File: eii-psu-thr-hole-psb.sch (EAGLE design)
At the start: 30 parts, among them IC2 7812TV

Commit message: Switched to through-hole resistors too
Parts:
- +15V, +5V, -15V, G, GND, L, N: value (none) -> PIN2F061.100; device SparkFun-Connectors:CONN_01PTH_2MM -> con-faston:PIN2F061.100
- R1, R2, R3, R4: device rcl:R-EU_R1206 -> rcl:R-EU_0207/7
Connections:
- new net G: G.1, X2-7.S
- net GND: no longer G.1, X2-7.S
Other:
- note added: "C86469"

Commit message: New heat sinks, better silk screen
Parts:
- KK1, KK2, KK3: value SK95V -> HEATSINKXSD; device joakim:SK95V -> joakim:HEATSINKXSD
- renumbered U$1 to IC1, U$2 to IC3
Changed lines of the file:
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@@
 <parts>
 <part name="IC2" library="linear" library_urn="urn:adsk.eagle:library:262" deviceset="78*" device="TV" package3d_urn="urn:adsk.eagle:package:16417/2" technology="12" value="7812TV"/>
-<part name="U$1" library="joakim" deviceset="LD1085V" device="3" value="LD1085V3"/>
-<part name="U$2" library="joakim" deviceset="LM2991" device="V" value="LM2991V"/>
+<part name="IC1" library="joakim" deviceset="LD1085V" device="3" value="LD1085V3"/>
+<part name="IC3" library="joakim" deviceset="LM2991" device="V" value="LM2991V"/>
 <part name="C1" library="rcl" library_urn="urn:adsk.eagle:library:334" deviceset="CPOL-US" device="E5-10.5" package3d_urn="urn:adsk.eagle:package:23372/2" value="470uF"/>
 <part name="C2" library="rcl" library_urn="urn:adsk.eagle:library:334" deviceset="CPOL-US" device="E5-10.5" package3d_urn="urn:adsk.eagle:package:23372/2" value="470uF"/>
@@
 <part name="GND" library="con-faston" library_urn="urn:adsk.eagle:library:144" deviceset="PIN2" device="F061.100" package3d_urn="urn:adsk.eagle:package:6758/1"/>
 <part name="GND15" library="supply1" library_urn="urn:adsk.eagle:library:371" deviceset="GND" device=""/>
-<part name="KK1" library="joakim" deviceset="SK95" device="V"/>
-<part name="KK2" library="joakim" deviceset="SK95" device="V"/>
-<part name="KK3" library="joakim" deviceset="SK95" device="V"/>
+<part name="KK1" library="joakim" deviceset="HEATSINK" device="XSD"/>
+<part name="KK2" library="joakim" deviceset="HEATSINK" device="XSD"/>
+<part name="KK3" library="joakim" deviceset="HEATSINK" device="XSD"/>
 </parts>
 <sheets>
@@
 <attribute name="VALUE" x="55.88" y="61.595" size="1.778" layer="96"/>
 </instance>
-<instance part="U$1" gate="G$1" x="63.5" y="101.6" smashed="yes">
+<instance part="IC1" gate="G$1" x="63.5" y="101.6" smashed="yes">
 <attribute name="NAME" x="55.88" y="107.315" size="1.778" layer="95"/>
 <attribute name="VALUE" x="55.88" y="104.775" size="1.778" layer="96"/>
 </instance>
-<instance part="U$2" gate="G$1" x="63.5" y="27.94" smashed="yes">
+<instance part="IC3" gate="G$1" x="63.5" y="27.94" smashed="yes">
 <attribute name="NAME" x="55.88" y="33.655" size="1.778" layer="95"/>
 <attribute name="VALUE" x="55.88" y="31.115" size="1.778" layer="96"/>
@@
 <net name="N$6" class="0">
 <segment>
-<pinref part="U$2" gate="G$1" pin="ADJ"/>
+<pinref part="IC3" gate="G$1" pin="ADJ"/>
 <wire x1="68.58" y1="20.32" x2="68.58" y2="7.62" width="0.1524" layer="91"/>
 <pinref part="R6" gate="G$1" pin="1"/>
@@
 </segment>
 <segment>
-<pinref part="U$2" gate="G$1" pin="GND"/>
+<pinref part="IC3" gate="G$1" pin="GND"/>
 <pinref part="GND3" gate="1" pin="GND"/>
 </segment>
 <segment>
-<pinref part="U$2" gate="G$1" pin="ON"/>
+<pinref part="IC3" gate="G$1" pin="ON"/>
 <pinref part="GND4" gate="1" pin="GND"/>
 </segment>
@@
 <net name="-15V" class="0">
 <segment>
-<pinref part="U$2" gate="G$1" pin="VI"/>
+<pinref part="IC3" gate="G$1" pin="VI"/>
 <pinref part="C9" gate="G$1" pin="1"/>
 <wire x1="53.34" y1="27.94" x2="43.18" y2="27.94" width="0.1524" layer="91"/>
@@
 <pinref part="C7" gate="G$1" pin="1"/>
 <wire x1="30.48" y1="101.6" x2="43.18" y2="101.6" width="0.1524" layer="91"/>
-<pinref part="U$1" gate="G$1" pin="VI"/>
+<pinref part="IC1" gate="G$1" pin="VI"/>
 <wire x1="43.18" y1="101.6" x2="53.34" y2="101.6" width="0.1524" layer="91"/>
 <junction x="43.18" y="101.6"/>
@@
 </segment>
 <segment>
-<pinref part="U$2" gate="G$1" pin="VO"/>
+<pinref part="IC3" gate="G$1" pin="VO"/>
 <pinref part="R3" gate="G$1" pin="2"/>
 <wire x1="73.66" y1="27.94" x2="78.74" y2="27.94" width="0.1524" layer="91"/>
@@
 </segment>
 <segment>
-<pinref part="U$1" gate="G$1" pin="VO"/>
+<pinref part="IC1" gate="G$1" pin="VO"/>
 <pinref part="R2" gate="G$1" pin="2"/>
 <wire x1="73.66" y1="101.6" x2="78.74" y2="101.6" width="0.1524" layer="91"/>
@@
 <net name="N$2" class="0">
 <segment>
-<pinref part="U$1" gate="G$1" pin="ADJ"/>
+<pinref part="IC1" gate="G$1" pin="ADJ"/>
 <pinref part="R5" gate="G$1" pin="1"/>
 <wire x1="63.5" y1="93.98" x2="63.5" y2="91.44" width="0.1524" layer="91"/>

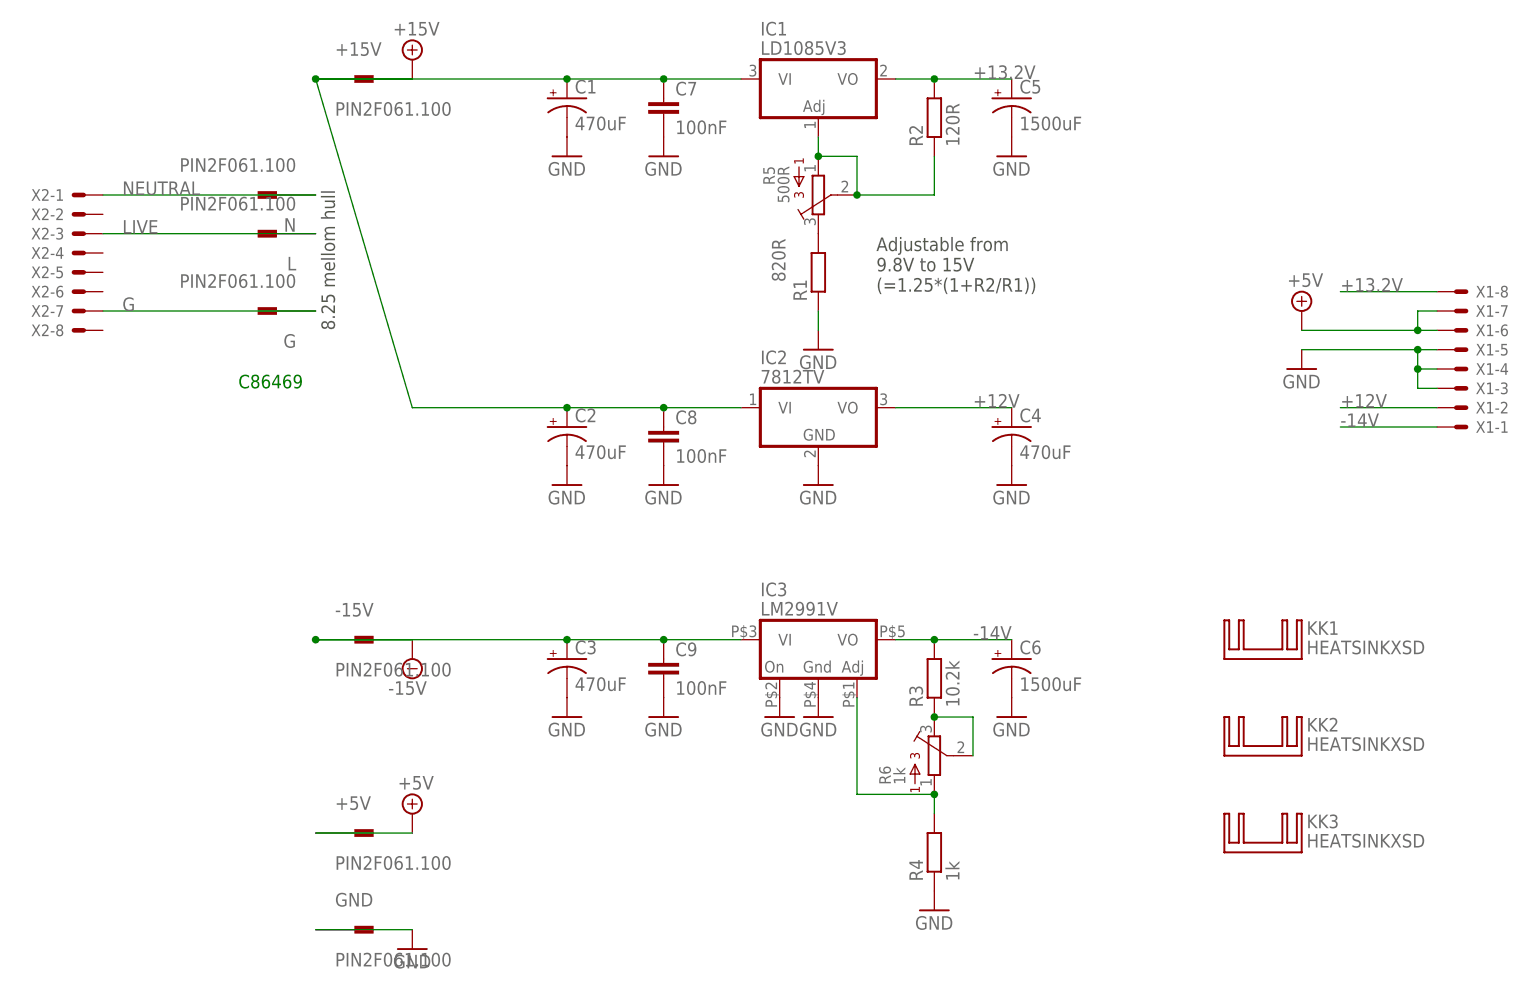
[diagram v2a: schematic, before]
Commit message: Added all parts except regulators
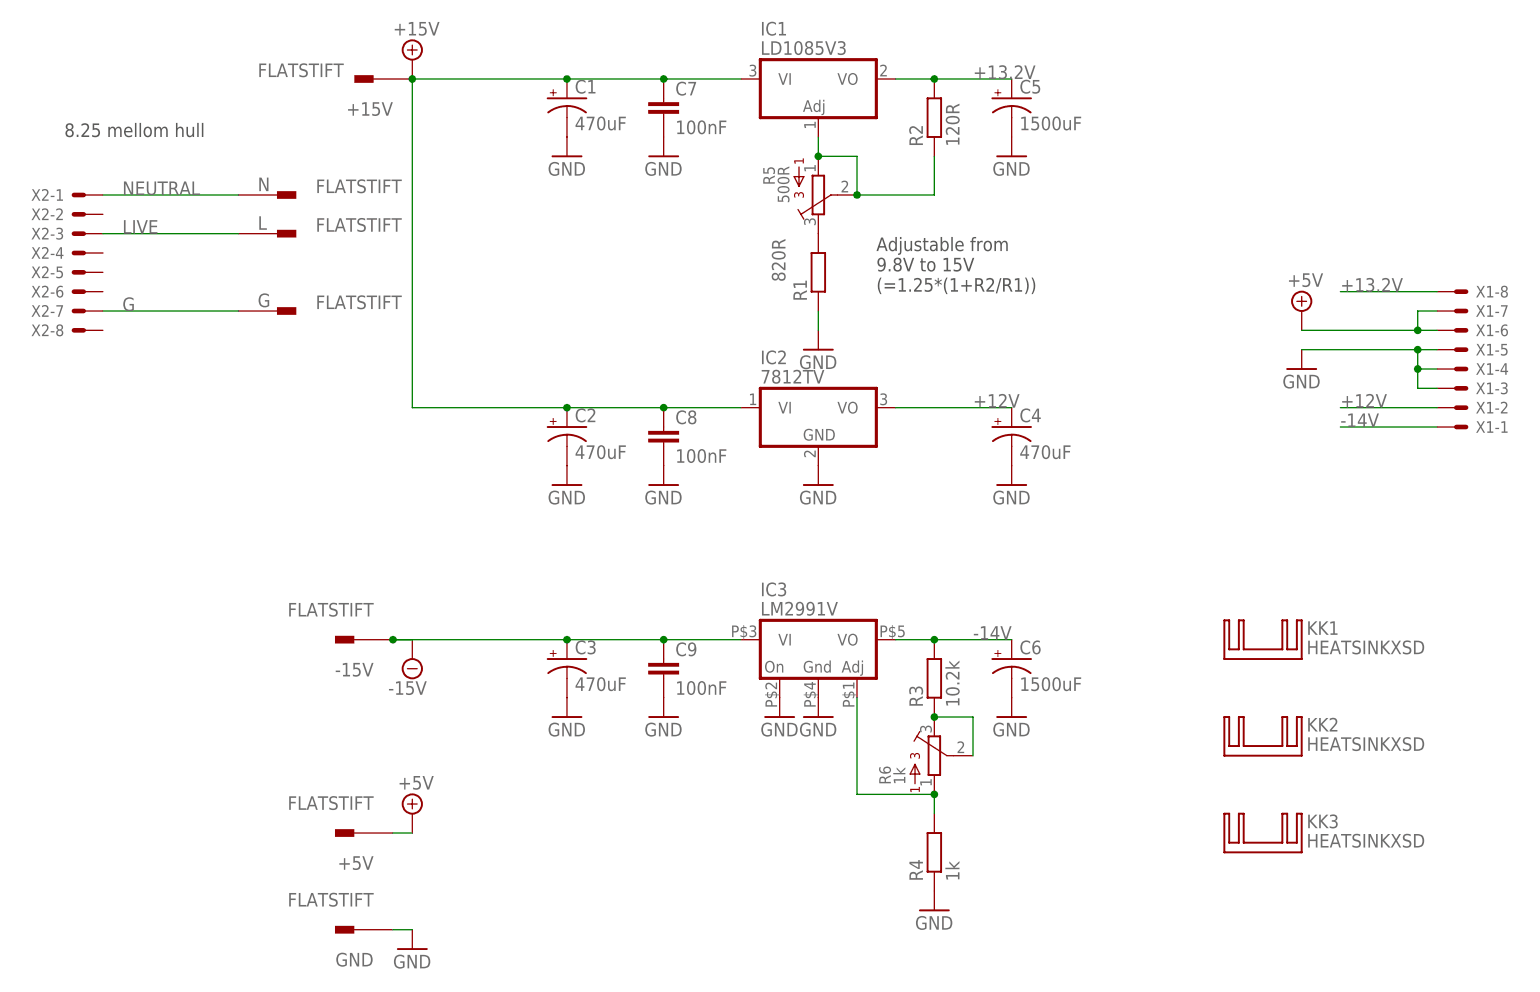
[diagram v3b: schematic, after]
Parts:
- +15V, +5V, -15V, G, GND, L, N: value PIN2F061.100 -> FLATSTIFT; device con-faston:PIN2F061.100 -> joakim:FLATSTIFT
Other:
- note removed: "C86469"
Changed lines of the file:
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@@
 <part name="SUPPLY3" library="supply2" library_urn="urn:adsk.eagle:library:372" deviceset="+15V" device=""/>
 <part name="SUPPLY4" library="supply2" library_urn="urn:adsk.eagle:library:372" deviceset="-15V" device=""/>
-<part name="N" library="con-faston" library_urn="urn:adsk.eagle:library:144" deviceset="PIN2" device="F061.100" package3d_urn="urn:adsk.eagle:package:6758/1"/>
-<part name="L" library="con-faston" library_urn="urn:adsk.eagle:library:144" deviceset="PIN2" device="F061.100" package3d_urn="urn:adsk.eagle:package:6758/1"/>
-<part name="G" library="con-faston" library_urn="urn:adsk.eagle:library:144" deviceset="PIN2" device="F061.100" package3d_urn="urn:adsk.eagle:package:6758/1"/>
-<part name="+15V" library="con-faston" library_urn="urn:adsk.eagle:library:144" deviceset="PIN2" device="F061.100" package3d_urn="urn:adsk.eagle:package:6758/1"/>
-<part name="-15V" library="con-faston" library_urn="urn:adsk.eagle:library:144" deviceset="PIN2" device="F061.100" package3d_urn="urn:adsk.eagle:package:6758/1"/>
-<part name="+5V" library="con-faston" library_urn="urn:adsk.eagle:library:144" deviceset="PIN2" device="F061.100" package3d_urn="urn:adsk.eagle:package:6758/1"/>
-<part name="GND" library="con-faston" library_urn="urn:adsk.eagle:library:144" deviceset="PIN2" device="F061.100" package3d_urn="urn:adsk.eagle:package:6758/1"/>
+<part name="N" library="joakim" deviceset="FLATSTIFT" device=""/>
+<part name="L" library="joakim" deviceset="FLATSTIFT" device=""/>
+<part name="G" library="joakim" deviceset="FLATSTIFT" device=""/>
+<part name="+15V" library="joakim" deviceset="FLATSTIFT" device=""/>
+<part name="-15V" library="joakim" deviceset="FLATSTIFT" device=""/>
+<part name="+5V" library="joakim" deviceset="FLATSTIFT" device=""/>
+<part name="GND" library="joakim" deviceset="FLATSTIFT" device=""/>
 <part name="GND15" library="supply1" library_urn="urn:adsk.eagle:library:371" deviceset="GND" device=""/>
 <part name="KK1" library="joakim" deviceset="HEATSINK" device="XSD"/>
@@
 9.8V to 15V
 (=1.25*(1+R2/R1))</text>
-<text x="0" y="68.58" size="1.778" layer="97" rot="R90">8.25 mellom hull</text>
-<text x="-12.7" y="60.96" size="1.778" layer="91">C86469</text>
+<text x="-35.56" y="93.98" size="1.778" layer="97">8.25 mellom hull</text>
 </plain>
 <instances>
@@
 <attribute name="VALUE" x="6.985" y="20.701" size="1.778" layer="96"/>
 </instance>
-<instance part="N" gate="-1" x="-7.62" y="86.36" smashed="yes" rot="R180">
-<attribute name="VALUE" x="-5.08" y="91.186" size="1.778" layer="96" font="vector" rot="R180"/>
-<attribute name="NAME" x="-5.08" y="83.312" size="1.778" layer="95" font="vector" rot="R180"/>
-</instance>
-<instance part="L" gate="-1" x="-7.62" y="81.28" smashed="yes" rot="R180">
-<attribute name="VALUE" x="-5.08" y="86.106" size="1.778" layer="96" font="vector" rot="R180"/>
-<attribute name="NAME" x="-5.08" y="78.232" size="1.778" layer="95" font="vector" rot="R180"/>
-</instance>
-<instance part="G" gate="-1" x="-7.62" y="71.12" smashed="yes" rot="R180">
-<attribute name="VALUE" x="-5.08" y="75.946" size="1.778" layer="96" font="vector" rot="R180"/>
-<attribute name="NAME" x="-5.08" y="68.072" size="1.778" layer="95" font="vector" rot="R180"/>
-</instance>
-<instance part="+15V" gate="-1" x="2.54" y="101.6" smashed="yes">
-<attribute name="VALUE" x="0" y="96.774" size="1.778" layer="96" font="vector"/>
-<attribute name="NAME" x="0" y="104.648" size="1.778" layer="95" font="vector"/>
-</instance>
-<instance part="-15V" gate="-1" x="2.54" y="27.94" smashed="yes">
-<attribute name="VALUE" x="0" y="23.114" size="1.778" layer="96" font="vector"/>
-<attribute name="NAME" x="0" y="30.988" size="1.778" layer="95" font="vector"/>
-</instance>
-<instance part="+5V" gate="-1" x="2.54" y="2.54" smashed="yes">
-<attribute name="VALUE" x="0" y="-2.286" size="1.778" layer="96" font="vector"/>
-<attribute name="NAME" x="0" y="5.588" size="1.778" layer="95" font="vector"/>
-</instance>
-<instance part="GND" gate="-1" x="2.54" y="-10.16" smashed="yes">
-<attribute name="VALUE" x="0" y="-14.986" size="1.778" layer="96" font="vector"/>
-<attribute name="NAME" x="0" y="-7.112" size="1.778" layer="95" font="vector"/>
+<instance part="N" gate="G$1" x="-7.62" y="86.36" smashed="yes">
+<attribute name="VALUE" x="-2.54" y="86.614" size="1.778" layer="96" font="vector"/>
+<attribute name="NAME" x="-10.16" y="86.868" size="1.778" layer="95" font="vector"/>
+</instance>
+<instance part="L" gate="G$1" x="-7.62" y="81.28" smashed="yes">
+<attribute name="VALUE" x="-2.54" y="81.534" size="1.778" layer="96" font="vector"/>
+<attribute name="NAME" x="-10.16" y="81.788" size="1.778" layer="95" font="vector"/>
+</instance>
+<instance part="G" gate="G$1" x="-7.62" y="71.12" smashed="yes">
+<attribute name="VALUE" x="-2.54" y="71.374" size="1.778" layer="96" font="vector"/>
+<attribute name="NAME" x="-10.16" y="71.628" size="1.778" layer="95" font="vector"/>
+</instance>
+<instance part="+15V" gate="G$1" x="5.08" y="101.6" smashed="yes" rot="R180">
+<attribute name="VALUE" x="-10.16" y="101.854" size="1.778" layer="96" font="vector"/>
+<attribute name="NAME" x="7.62" y="98.552" size="1.778" layer="95" font="vector" rot="R180"/>
+</instance>
+<instance part="-15V" gate="G$1" x="2.54" y="27.94" smashed="yes" rot="R180">
+<attribute name="VALUE" x="5.08" y="32.766" size="1.778" layer="96" font="vector" rot="R180"/>
+<attribute name="NAME" x="5.08" y="24.892" size="1.778" layer="95" font="vector" rot="R180"/>
+</instance>
+<instance part="+5V" gate="G$1" x="2.54" y="2.54" smashed="yes" rot="R180">
+<attribute name="VALUE" x="5.08" y="7.366" size="1.778" layer="96" font="vector" rot="R180"/>
+<attribute name="NAME" x="5.08" y="-0.508" size="1.778" layer="95" font="vector" rot="R180"/>
+</instance>
+<instance part="GND" gate="G$1" x="2.54" y="-10.16" smashed="yes" rot="R180">
+<attribute name="VALUE" x="5.08" y="-5.334" size="1.778" layer="96" font="vector" rot="R180"/>
+<attribute name="NAME" x="5.08" y="-13.208" size="1.778" layer="95" font="vector" rot="R180"/>
 </instance>
 <instance part="GND15" gate="1" x="10.16" y="-12.7" smashed="yes">
@@
 </segment>
 <segment>
-<pinref part="GND" gate="-1" pin="1"/>
+<pinref part="GND" gate="G$1" pin="1"/>
 <pinref part="GND15" gate="1" pin="GND"/>
-<wire x1="10.16" y1="-10.16" x2="-2.54" y2="-10.16" width="0.1524" layer="91"/>
+<wire x1="10.16" y1="-10.16" x2="7.62" y2="-10.16" width="0.1524" layer="91"/>
 </segment>
 <segment>
@@
 <wire x1="43.18" y1="27.94" x2="30.48" y2="27.94" width="0.1524" layer="91"/>
 <junction x="43.18" y="27.94"/>
-<wire x1="30.48" y1="27.94" x2="-2.54" y2="27.94" width="0.1524" layer="91"/>
+<wire x1="30.48" y1="27.94" x2="7.62" y2="27.94" width="0.1524" layer="91"/>
 <junction x="30.48" y="27.94"/>
 <pinref part="SUPPLY4" gate="G$1" pin="-15V"/>
-<pinref part="-15V" gate="-1" pin="1"/>
-<junction x="-2.54" y="27.94"/>
-<wire x1="10.16" y1="27.94" x2="-2.54" y2="27.94" width="0.1524" layer="91"/>
+<pinref part="-15V" gate="G$1" pin="1"/>
+<junction x="7.62" y="27.94"/>
+<wire x1="10.16" y1="27.94" x2="7.62" y2="27.94" width="0.1524" layer="91"/>
 </segment>
 </net>
@@
 <wire x1="30.48" y1="58.42" x2="10.16" y2="58.42" width="0.1524" layer="91"/>
 <junction x="30.48" y="58.42"/>
-<wire x1="10.16" y1="58.42" x2="-2.54" y2="101.6" width="0.1524" layer="91"/>
+<wire x1="10.16" y1="58.42" x2="10.16" y2="101.6" width="0.1524" layer="91"/>
 <pinref part="C1" gate="G$1" pin="+"/>
 <pinref part="C7" gate="G$1" pin="1"/>
@@
 <wire x1="43.18" y1="101.6" x2="53.34" y2="101.6" width="0.1524" layer="91"/>
 <junction x="43.18" y="101.6"/>
-<wire x1="-2.54" y1="101.6" x2="30.48" y2="101.6" width="0.1524" layer="91"/>
+<wire x1="10.16" y1="101.6" x2="30.48" y2="101.6" width="0.1524" layer="91"/>
 <junction x="30.48" y="101.6"/>
 <pinref part="SUPPLY3" gate="+15V" pin="+15V"/>
-<junction x="-2.54" y="101.6"/>
-<pinref part="+15V" gate="-1" pin="1"/>
-<wire x1="10.16" y1="101.6" x2="-2.54" y2="101.6" width="0.1524" layer="91"/>
+<junction x="10.16" y="101.6"/>
+<pinref part="+15V" gate="G$1" pin="1"/>
 </segment>
 </net>
@@
 </segment>
 <segment>
-<pinref part="+5V" gate="-1" pin="1"/>
+<pinref part="+5V" gate="G$1" pin="1"/>
 <pinref part="SUPPLY2" gate="+5V" pin="+5V"/>
-<wire x1="10.16" y1="2.54" x2="-2.54" y2="2.54" width="0.1524" layer="91"/>
+<wire x1="10.16" y1="2.54" x2="7.62" y2="2.54" width="0.1524" layer="91"/>
 </segment>
 </net>
@@
 <net name="NEUTRAL" class="0">
 <segment>
-<wire x1="-30.48" y1="86.36" x2="-2.54" y2="86.36" width="0.1524" layer="91"/>
+<wire x1="-30.48" y1="86.36" x2="-12.7" y2="86.36" width="0.1524" layer="91"/>
 <label x="-27.94" y="86.36" size="1.778" layer="95"/>
-<pinref part="N" gate="-1" pin="1"/>
+<pinref part="N" gate="G$1" pin="1"/>
 <pinref part="X2" gate="-1" pin="S"/>
 </segment>
@@
 <segment>
 <pinref part="X2" gate="-3" pin="S"/>
-<pinref part="L" gate="-1" pin="1"/>
-<wire x1="-30.48" y1="81.28" x2="-2.54" y2="81.28" width="0.1524" layer="91"/>
+<pinref part="L" gate="G$1" pin="1"/>
+<wire x1="-30.48" y1="81.28" x2="-12.7" y2="81.28" width="0.1524" layer="91"/>
 <label x="-27.94" y="81.28" size="1.778" layer="95"/>
 </segment>
@@
 <net name="G" class="0">
 <segment>
-<pinref part="G" gate="-1" pin="1"/>
+<pinref part="G" gate="G$1" pin="1"/>
 <pinref part="X2" gate="-7" pin="S"/>
-<wire x1="-2.54" y1="71.12" x2="-30.48" y2="71.12" width="0.1524" layer="91"/>
+<wire x1="-12.7" y1="71.12" x2="-30.48" y2="71.12" width="0.1524" layer="91"/>
 <label x="-27.94" y="71.12" size="1.778" layer="95"/>
 </segment>
